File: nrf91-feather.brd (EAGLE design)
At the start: 50.8 x 22.9 mm, 123 parts, among them J2 CON-HEADER-1X12-MALE-PIN, J3 CON-HEADER-1X16-MALE-PIN, J4 CON-1909763-1, J5 CON-SIM-104224-0820, J6 CON-S2B-PH-SM4-TB(LF)(SN), J7 CON-1909763-1, J8 CON-USB-DX07S016JA1R1500, J9 CON-TC2030-MCP-NL, Q2 MOSFET-DUAL-COMP-SOT563, Q3 MOSFET-P-20V-4.7A-SOT23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

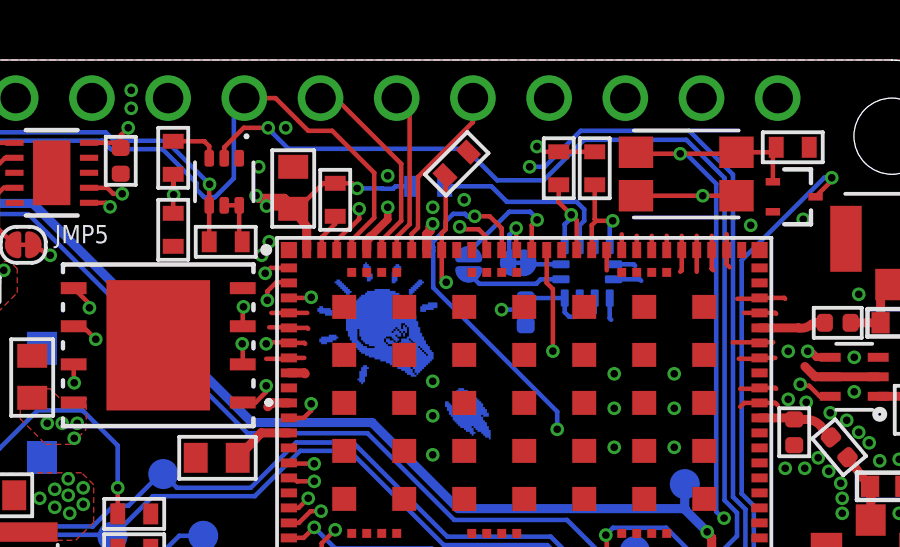
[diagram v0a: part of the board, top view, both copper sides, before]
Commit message: Minor clean up
Changed:
* Bottom layer trace/ground fix
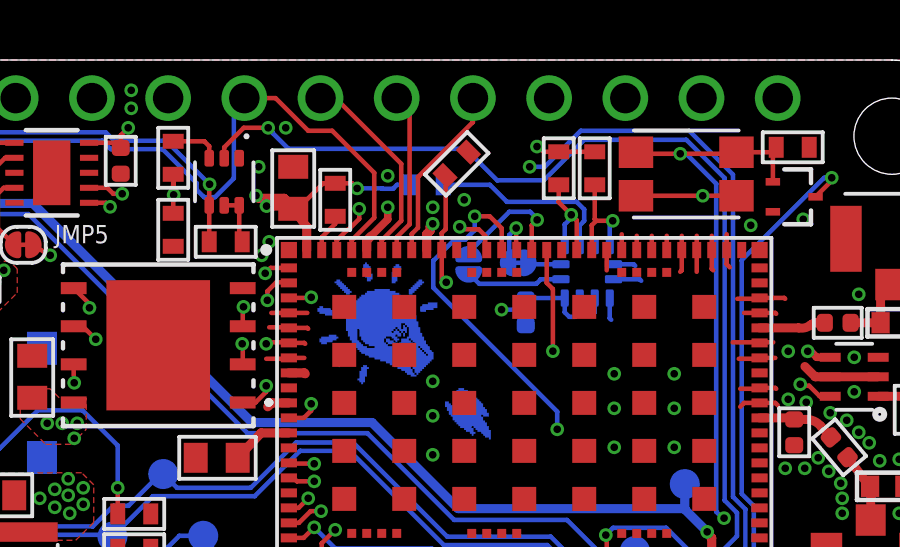
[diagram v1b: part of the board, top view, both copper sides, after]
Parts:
- moved R20 0.07 mm to (32.8, 18.7)
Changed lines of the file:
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@@
 <grid distance="0.05" unitdist="mm" unit="mm" style="lines" multiple="1" display="yes" altdistance="0.1" altunitdist="mm" altunit="mm"/>
 <layers>
-<layer number="1" name="Top" color="4" fill="1" visible="yes" active="yes"/>
+<layer number="1" name="Top" color="4" fill="1" visible="no" active="yes"/>
 <layer number="2" name="Route2" color="24" fill="1" visible="no" active="yes"/>
 <layer number="3" name="Route3" color="4" fill="3" visible="no" active="no"/>
@@
 <layer number="14" name="Route14" color="1" fill="6" visible="no" active="yes"/>
 <layer number="15" name="Route15" color="32" fill="1" visible="no" active="yes"/>
-<layer number="16" name="Bottom" color="1" fill="1" visible="no" active="yes"/>
+<layer number="16" name="Bottom" color="1" fill="1" visible="yes" active="yes"/>
 <layer number="17" name="Pads" color="2" fill="1" visible="yes" active="yes"/>
 <layer number="18" name="Vias" color="2" fill="1" visible="yes" active="yes"/>
 <layer number="19" name="Unrouted" color="6" fill="1" visible="yes" active="yes"/>
 <layer number="20" name="Dimension" color="15" fill="1" visible="yes" active="yes"/>
-<layer number="21" name="tPlace" color="14" fill="1" visible="yes" active="yes"/>
-<layer number="22" name="bPlace" color="14" fill="1" visible="no" active="yes"/>
-<layer number="23" name="tOrigins" color="14" fill="1" visible="yes" active="yes"/>
-<layer number="24" name="bOrigins" color="13" fill="1" visible="no" active="yes"/>
-<layer number="25" name="tNames" color="7" fill="1" visible="yes" active="yes"/>
-<layer number="26" name="bNames" color="7" fill="1" visible="no" active="yes"/>
+<layer number="21" name="tPlace" color="14" fill="1" visible="no" active="yes"/>
+<layer number="22" name="bPlace" color="14" fill="1" visible="yes" active="yes"/>
+<layer number="23" name="tOrigins" color="14" fill="1" visible="no" active="yes"/>
+<layer number="24" name="bOrigins" color="13" fill="1" visible="yes" active="yes"/>
+<layer number="25" name="tNames" color="7" fill="1" visible="no" active="yes"/>
+<layer number="26" name="bNames" color="7" fill="1" visible="yes" active="yes"/>
 <layer number="27" name="tValues" color="7" fill="1" visible="no" active="yes"/>
 <layer number="28" name="bValues" color="7" fill="1" visible="no" active="yes"/>
@@
 <layer number="37" name="tTest" color="7" fill="1" visible="no" active="yes"/>
 <layer number="38" name="bTest" color="7" fill="1" visible="no" active="yes"/>
-<layer number="39" name="tKeepout" color="4" fill="11" visible="yes" active="yes"/>
-<layer number="40" name="bKeepout" color="1" fill="11" visible="no" active="yes"/>
-<layer number="41" name="tRestrict" color="4" fill="10" visible="yes" active="yes"/>
-<layer number="42" name="bRestrict" color="1" fill="10" visible="no" active="yes"/>
+<layer number="39" name="tKeepout" color="4" fill="11" visible="no" active="yes"/>
+<layer number="40" name="bKeepout" color="1" fill="11" visible="yes" active="yes"/>
+<layer number="41" name="tRestrict" color="4" fill="10" visible="no" active="yes"/>
+<layer number="42" name="bRestrict" color="1" fill="10" visible="yes" active="yes"/>
 <layer number="43" name="vRestrict" color="2" fill="10" visible="no" active="yes"/>
 <layer number="44" name="Drills" color="7" fill="1" visible="no" active="yes"/>
@@
 <layer number="50" name="dxf" color="7" fill="1" visible="no" active="no"/>
 <layer number="51" name="tDocu" color="7" fill="1" visible="no" active="yes"/>
-<layer number="52" name="bDocu" color="7" fill="1" visible="no" active="yes"/>
+<layer number="52" name="bDocu" color="7" fill="1" visible="yes" active="yes"/>
 <layer number="53" name="tGND_GNDA" color="7" fill="9" visible="no" active="no"/>
 <layer number="54" name="bGND_GNDA" color="1" fill="9" visible="no" active="no"/>
@@
 <element name="U$15" library="buzzard_labels-17" package="#RST0" value="" x="6.37" y="1.413840625" smashed="yes" rot="MR90"/>
 <element name="U$23" library="buzzard_labels-11" package="RST0" value="" x="34.15" y="3.7" smashed="yes"/>
-<element name="R20" library="wolff-den" library_urn="urn:adsk.eagle:library:6370453" package="R0402-M" package3d_urn="urn:adsk.eagle:package:19061974/5" value="100k" x="32.8" y="18.65" smashed="yes" rot="MR0">
-<attribute name="DESC" value="RES SMD 100K OHM 1% 1/16W 0402" x="32.8" y="18.65" size="1.778" layer="28" rot="MR0" display="off"/>
-<attribute name="DIGIKEYPN" value="311-100KLRCT-ND" x="32.8" y="18.65" size="1.778" layer="28" rot="MR0" display="off"/>
-<attribute name="MF" value="" x="32.8" y="18.65" size="1.778" layer="28" rot="MR0" display="off"/>
-<attribute name="MPN" value="RC0402FR07100KL" x="32.8" y="18.65" size="1.778" layer="28" rot="MR0" display="off"/>
-<attribute name="NAME" x="32.8" y="18.65" size="0.2" layer="52" rot="MR0" align="center"/>
-<attribute name="POWER" value="1/16W" x="32.8" y="18.65" size="1.778" layer="28" rot="MR0" display="off"/>
-<attribute name="TEMPHIGH" value="" x="32.8" y="18.65" size="1.778" layer="28" rot="MR0" display="off"/>
-<attribute name="TEMPLOW" value="" x="32.8" y="18.65" size="1.778" layer="28" rot="MR0" display="off"/>
-<attribute name="TOLERANCE" value="1%" x="32.8" y="18.65" size="1.778" layer="28" rot="MR0" display="off"/>
+<element name="R20" library="wolff-den" library_urn="urn:adsk.eagle:library:6370453" package="R0402-M" package3d_urn="urn:adsk.eagle:package:19061974/5" value="100k" x="32.75" y="18.7" smashed="yes" rot="MR0">
+<attribute name="DESC" value="RES SMD 100K OHM 1% 1/16W 0402" x="32.75" y="18.7" size="1.778" layer="28" rot="MR0" display="off"/>
+<attribute name="DIGIKEYPN" value="311-100KLRCT-ND" x="32.75" y="18.7" size="1.778" layer="28" rot="MR0" display="off"/>
+<attribute name="MF" value="" x="32.75" y="18.7" size="1.778" layer="28" rot="MR0" display="off"/>
+<attribute name="MPN" value="RC0402FR07100KL" x="32.75" y="18.7" size="1.778" layer="28" rot="MR0" display="off"/>
+<attribute name="NAME" x="32.75" y="18.7" size="0.2" layer="52" rot="MR0" align="center"/>
+<attribute name="POWER" value="1/16W" x="32.75" y="18.7" size="1.778" layer="28" rot="MR0" display="off"/>
+<attribute name="TEMPHIGH" value="" x="32.75" y="18.7" size="1.778" layer="28" rot="MR0" display="off"/>
+<attribute name="TEMPLOW" value="" x="32.75" y="18.7" size="1.778" layer="28" rot="MR0" display="off"/>
+<attribute name="TOLERANCE" value="1%" x="32.75" y="18.7" size="1.778" layer="28" rot="MR0" display="off"/>
 </element>
 <element name="ASSEMBLY1" library="wolff-den" library_urn="urn:adsk.eagle:library:6370453" package="PLACEHOLDER" package3d_urn="urn:adsk.eagle:package:10610054/3" value="ASSY-COST-NRF91-FEATHER" x="-173.5" y="-117.3" smashed="yes">
@@
 <via x="20.850003125" y="7.750003125" extent="1-16" drill="0.254"/>
 <via x="30.43033125" y="18.58033125" extent="1-16" drill="0.254"/>
-<wire x1="32.25" y1="18.65" x2="31.7106625" y2="18.65" width="0.1524" layer="16"/>
-<wire x1="31.7106625" y1="18.65" x2="31.6288625" y2="18.5682" width="0.1524" layer="16"/>
+<wire x1="32.2" y1="18.7" x2="31.7606625" y2="18.7" width="0.1524" layer="16"/>
+<wire x1="31.7606625" y1="18.7" x2="31.6288625" y2="18.5682" width="0.1524" layer="16"/>
 <wire x1="31.6288625" y1="18.5682" x2="31.2711375" y2="18.5682" width="0.1524" layer="16"/>
 <wire x1="31.2711375" y1="18.5682" x2="31.25900625" y2="18.58033125" width="0.1524" layer="16"/>
@@
 <wire x1="44.45" y1="1.27" x2="39.1268" y2="6.5932" width="0.1524" layer="2"/>
 <wire x1="39.1268" y1="6.5932" x2="38.5405375" y2="6.5932" width="0.1524" layer="2"/>
-<wire x1="32.9682" y1="16.6318" x2="32.95" y2="16.65" width="0.1524" layer="16"/>
-<wire x1="32.9682" y1="15.2711375" x2="32.9682" y2="16.5" width="0.1524" layer="16"/>
-<wire x1="32.9682" y1="16.5" x2="32.9682" y2="16.6318" width="0.1524" layer="16"/>
-<wire x1="33.3818" y1="17.2211375" x2="33.3818" y2="17.4818" width="0.1524" layer="16"/>
-<wire x1="32.95" y1="16.65" x2="32.95" y2="16.7893375" width="0.1524" layer="16"/>
-<wire x1="32.95" y1="16.7893375" x2="33.3818" y2="17.2211375" width="0.1524" layer="16"/>
-<wire x1="34.0288625" y1="17.7318" x2="34.1106625" y2="17.65" width="0.1524" layer="16"/>
-<wire x1="34.1106625" y1="17.65" x2="34.35" y2="17.65" width="0.1524" layer="16"/>
-<wire x1="33.6318" y1="17.7318" x2="34.0288625" y2="17.7318" width="0.1524" layer="16"/>
-<wire x1="33.3818" y1="17.4818" x2="33.6318" y2="17.7318" width="0.1524" layer="16"/>
 <wire x1="38.5405375" y1="6.5932" x2="37.1" y2="8.0337375" width="0.1524" layer="2"/>
 <wire x1="37.1" y1="8.0337375" x2="37.1" y2="10.55" width="0.1524" layer="2"/>
@@
 <wire x1="37.1" y1="11.1393375" x2="37.1" y2="10.55" width="0.1524" layer="16"/>
 <wire x1="37.1" y1="11.1393375" x2="32.9682" y2="15.2711375" width="0.1524" layer="16"/>
+<wire x1="32.9682" y1="15.2711375" x2="32.9682" y2="16.1682" width="0.1524" layer="16"/>
+<wire x1="33.6682" y1="16.8682" x2="34.0288625" y2="16.8682" width="0.1524" layer="16"/>
+<wire x1="34.0288625" y1="16.8682" x2="34.35" y2="17.1893375" width="0.1524" layer="16"/>
+<wire x1="34.35" y1="17.1893375" x2="34.35" y2="17.65" width="0.1524" layer="16"/>
+<wire x1="32.9682" y1="16.1682" x2="33.6682" y2="16.8682" width="0.1524" layer="16"/>
 </signal>
 <signal name="P0.21/COPI">
@@
 <wire x1="37.85" y1="17.35" x2="37.85" y2="16.675" width="0.1524" layer="16"/>
 <wire x1="38" y1="17.5" x2="37.85" y2="17.35" width="0.1524" layer="16"/>
-<wire x1="33.35" y1="18.65" x2="34.9048625" y2="18.65" width="0.1524" layer="16"/>
+<wire x1="33.3" y1="18.7" x2="34.8548625" y2="18.7" width="0.1524" layer="16"/>
 <wire x1="37.7470625" y1="18.1318" x2="38" y2="17.8788625" width="0.1524" layer="16"/>
-<wire x1="34.9048625" y1="18.65" x2="35.4230625" y2="18.1318" width="0.1524" layer="16"/>
+<wire x1="34.8548625" y1="18.7" x2="35.4230625" y2="18.1318" width="0.1524" layer="16"/>
 <wire x1="35.4230625" y1="18.1318" x2="37.7470625" y2="18.1318" width="0.1524" layer="16"/>
 <wire x1="38" y1="17.8788625" x2="38" y2="17.5" width="0.1524" layer="16"/>

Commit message: Cleanup
Changed:
* Improving ground paths
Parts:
- moved JMP4 0.25 mm to (19.2, 3.95)
- moved C10 0.22 mm to (19.7, 12.1)
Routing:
- net GND: track 57.5 -> 56.4 mm

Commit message: V5 Proto 1
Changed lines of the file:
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@@
 <layer number="49" name="Reference" color="7" fill="1" visible="no" active="yes"/>
 <layer number="50" name="dxf" color="7" fill="1" visible="no" active="no"/>
-<layer number="51" name="tDocu" color="7" fill="1" visible="yes" active="yes"/>
+<layer number="51" name="tDocu" color="7" fill="1" visible="no" active="yes"/>
 <layer number="52" name="bDocu" color="7" fill="1" visible="no" active="yes"/>
 <layer number="53" name="tGND_GNDA" color="7" fill="9" visible="no" active="no"/>
@@
 <wire x1="27.72" y1="14.43" x2="27.5" y2="14.21" width="0.254" layer="1"/>
 <wire x1="27.5" y1="14.21" x2="27.5" y2="13.95" width="0.254" layer="1"/>
-<wire x1="43.9" y1="11.45" x2="44.42" y2="11.45" width="0.254" layer="1"/>
-<wire x1="43.845" y1="11.43" x2="43.9" y2="11.45" width="0" layer="19" extent="1-1"/>
+<wire x1="43.9" y1="11.45" x2="44.05" y2="11.45" width="0.254" layer="1"/>
+<wire x1="44.05" y1="11.45" x2="44.42" y2="11.45" width="0.254" layer="1"/>
+<wire x1="43.845" y1="11.43" x2="43.865" y2="11.45" width="0.1524" layer="1"/>
+<wire x1="43.865" y1="11.45" x2="44.05" y2="11.45" width="0.1524" layer="1"/>
 </signal>
 <signal name="+3V3">

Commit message: Modifications
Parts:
- removed JMP4: JUMPER-NC, wolff-den:JUMPER-ROUND-NC
- removed Q5: MOSFET-N-SC89, wolff-den:DIO_RB558WMF-L
- removed R7: 1M, wolff-den:R0402-M
- added Q1: MOSFET-N-SC89, wolff-den:DIO_RB558WMF-L
- JMP5: value JUMPER-NC -> JUMPER-NO-ROUND-NO; device wolff-den:JUMPER-ROUND-NC -> wolff-den:JUMPER-ROUND-N0
- moved R5 10.4 mm to (25.2, 7.20), turned to 270 degrees
- moved R2 5.55 mm to (17.9, 4.25)
- moved R12 2.17 mm to (23.1, 9.90)
- moved R19 1.25 mm to (14.8, 4.80)
- moved JMP2 0.45 mm to (14.2, 11.4), turned to 270 degrees
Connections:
- removed net !EN: J2.2, Q5.1, R19.2
- removed net PS_EN: Q5.3, R5.1, U3.4
- removed net PS_MODE: JMP4.P$2, R7.2, U3.3
- new net EN: J2.2, R19.2, U3.4
- new net N$12: Q1.1, R5.2, U2.2
- net !RESET: now also Q1.3; no longer U2.2
- net GND: now also Q1.2, R5.1, U3.3; no longer Q5.2, R19.1, R7.1
- net P0.13/A0: no longer JMP4.P$1
- net VBUS: now also JMP2.P$1
- net VSYS: now also R19.1; no longer JMP2.P$1, R5.2
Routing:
- net !EN: track 24.2 -> 0.00 mm, vias 1 -> 0
- net EN: track 0.00 -> 24.0 mm, vias 0 -> 1
- net N$12: track 0.00 -> 23.6 mm, vias 0 -> 3
- net !RESET: track 55.9 -> 46.8 mm
- net N$1: track 5.67 -> 1.16 mm
- net PS_MODE: track 4.26 -> 0.00 mm
- net PS_EN: track 2.36 -> 0.00 mm
- net GND: track 56.7 -> 58.3 mm, vias 87 -> 88
- net VSYS: track 46.4 -> 47.8 mm
- net VBUS: track 47.6 -> 48.8 mm
- net MODE/WAKE: track 55.9 -> 54.8 mm
- net P0.13/A0: track 17.8 -> 16.8 mm, vias 2 -> 1

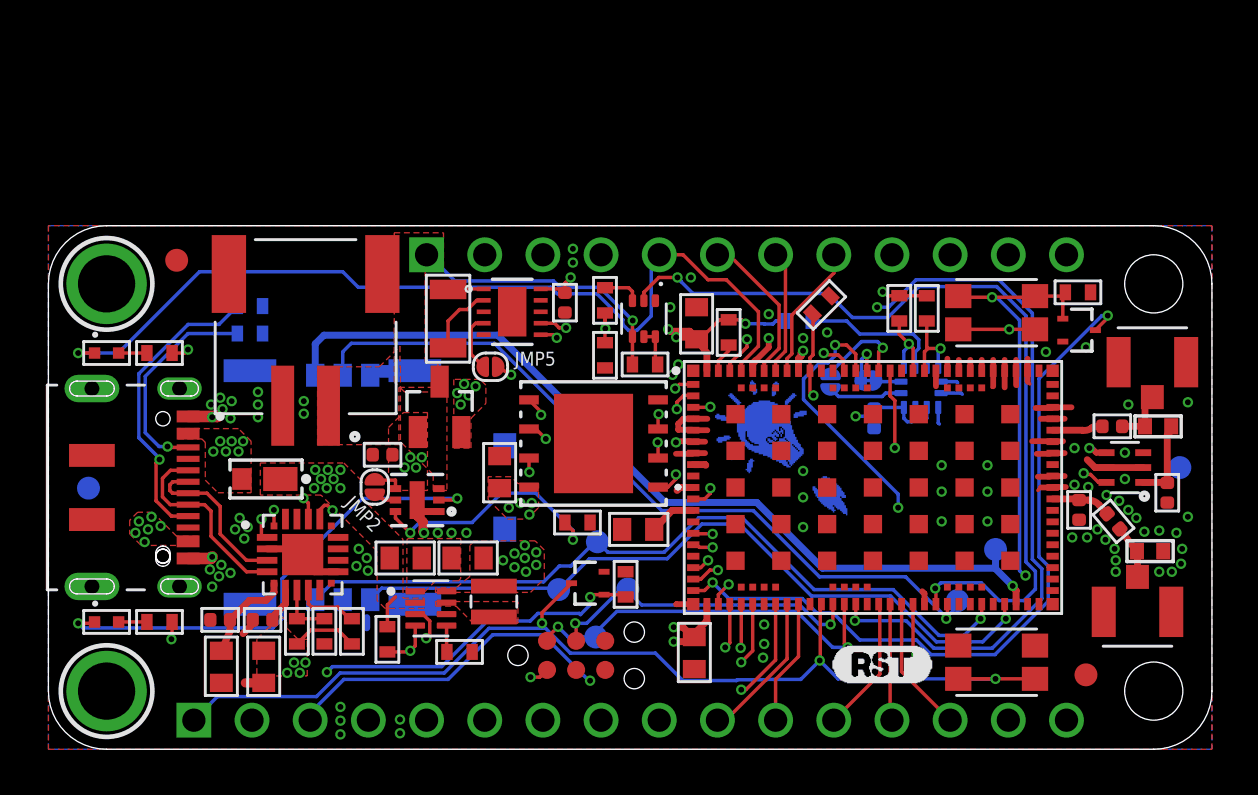
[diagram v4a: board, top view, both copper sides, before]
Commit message: Updating use of WP and HOLD pins
Changed
* Removed connections directly to mcu and replaced with pull-ups
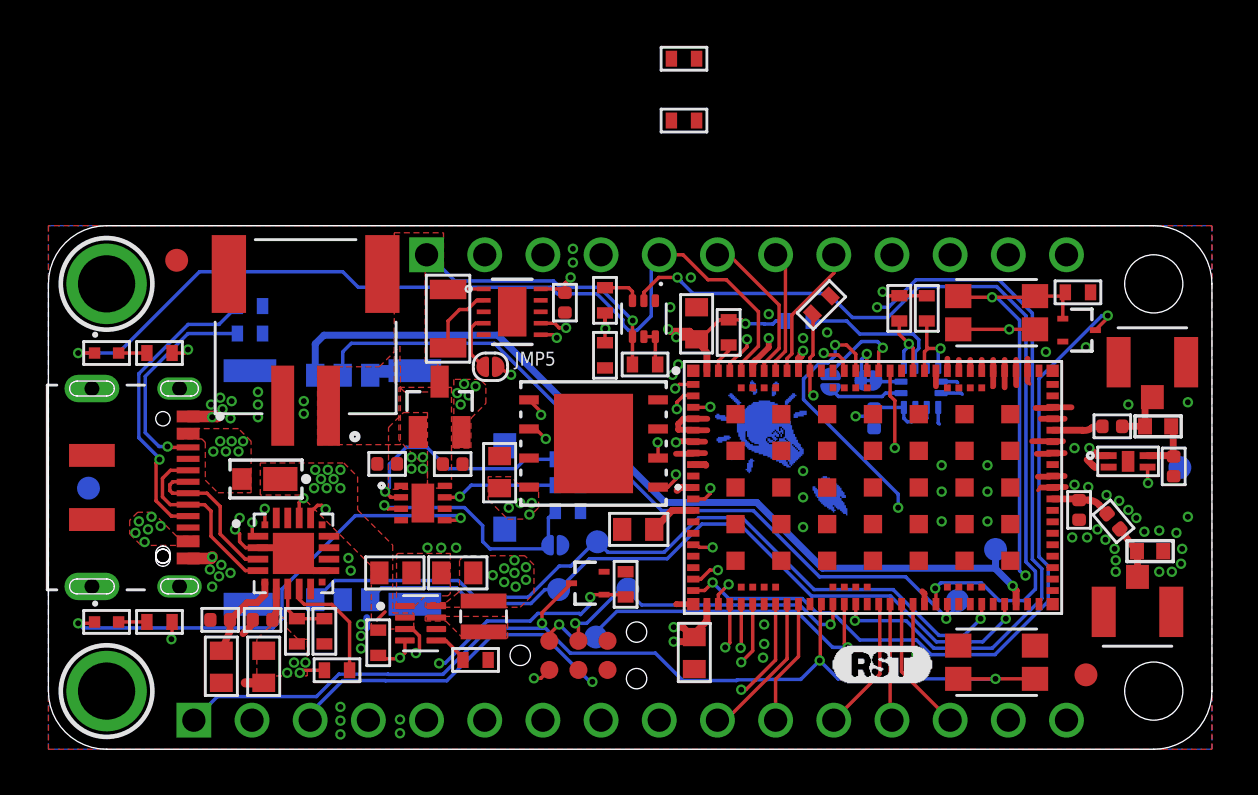
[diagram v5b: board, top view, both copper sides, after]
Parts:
- added C6: 1u, wolff-den:CAPC1005X55N
- added NTC1: 10k, wolff-den:R0402-M
- added R22, R23: 100k, wolff-den:R0402-M
- added R7: 27k, wolff-den:R0402-M
- R12: value 3.4k -> 1k
- R9: value 1M -> 100k
- U4: value POWER-SWITCH-MIC94092YC6 -> POWER-SWITCH-SIP32409-DFN4; device wolff-den:SOT363 -> wolff-den:SON50P160X120X60-5N
- U5: value IC-MCP73830T -> IC-BQ25170JDSGR-WSON8; device wolff-den:DFN6_2X2MY_MCH -> wolff-den:WSON8_BQ2517_TEX-L
- moved JMP2 8.28 mm to (22.1, 8.91), flipped to the bottom, turned to 180 degrees
- moved U$6 3.41 mm to (29.5, 13.4)
- moved R12 2.79 mm to (22.7, 12.7), flipped to the bottom, turned to 0 degrees
- moved R4 1.82 mm to (12.6, 3.45), turned to 180 degrees
- moved C19 1.18 mm to (49.1, 12.3)
- moved L2 0.79 mm to (19.0, 5.80)
- moved U3 0.79 mm to (16.2, 5.50)
- moved C4 0.79 mm to (17.9, 7.70)
- moved C5 0.79 mm to (15.2, 7.70)
- moved R2 0.78 mm to (18.6, 3.90)
- moved C11 0.45 mm to (14.8, 12.5)
- moved R19 0.43 mm to (14.4, 4.65)
- moved U2 0.40 mm to (10.7, 8.55)
- moved U4 0.30 mm to (47.1, 12.6), turned to 0 degrees
- moved U5 0.28 mm to (16.4, 10.8), turned to 0 degrees
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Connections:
- removed net CHRG: D4.C, U5.2
- removed net FLASH_HOLD: U1.18, U6.7
- removed net FLASH_WP: U1.15, U6.3
- removed net PROG: R12.2, U5.6
- new net CHG_ISET: R12.2, U5.2
- new net CHG_STAT: D4.C, U5.5
- new net CHG_TS: JMP2.P$1, NTC1.2, U5.3
- new net CHG_VSET: R7.2, U5.7
- new net N$14: R22.1, U6.7
- net +3V3: now also R22.2, R23.2, U4.1; no longer U4.4
- net COEX0/GPS_EN: now also U4.3; no longer U4.6
- net GND: now also C6.2, JMP2.P$2, NTC1.1, R7.1, U5.4, U5.9; no longer U5.1, U5.7
- net LNA_SW_OUT: now also U4.4; no longer U4.1
- net N$9: now also R23.1, U6.3; no longer JMP2.P$2, U5.5
- net VBAT: now also C6.1, U5.8; no longer U5.3
- net VBUS: now also U5.1; no longer JMP2.P$1, U5.4
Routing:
- net CHRG: track 21.6 -> 0.00 mm, vias 2 -> 0
- net CHG_STAT: track 0.00 -> 21.1 mm, vias 0 -> 2
- net PROG: track 11.0 -> 0.00 mm, vias 2 -> 0
- net FLASH_HOLD: track 10.9 -> 0.00 mm, vias 2 -> 0
- net CHG_TS: track 0.00 -> 10.8 mm, vias 0 -> 1
- net CHG_ISET: track 0.00 -> 10.2 mm, vias 0 -> 1
- net FLASH_WP: track 8.60 -> 0.00 mm, vias 2 -> 0
- net CHG_VSET: track 0.00 -> 5.05 mm, vias 0 -> 1
- net GND: track 58.3 -> 55.0 mm, vias 88 -> 84
- net VBUS: track 48.8 -> 45.7 mm
- net COEX0/GPS_EN: track 18.2 -> 21.2 mm
- net EN: track 24.0 -> 21.2 mm
- net CP2102N-!RST: track 2.77 -> 5.28 mm
- net N$12: track 23.6 -> 22.1 mm
- net LNA_SW_OUT: track 3.67 -> 2.52 mm
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- added copper zone on layer 2, net VBUS
